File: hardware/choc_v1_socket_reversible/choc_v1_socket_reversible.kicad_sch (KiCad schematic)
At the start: 76 parts, among them J1 Conn_01x12_MountingPin, J2 Conn_01x12_MountingPin, SW00 SW_Push, SW01 SW_Push, SW02 SW_Push, SW03 SW_Push, SW04 SW_Push, SW05 SW_Push, SW10 SW_Push, SW11 SW_Push, SW12 SW_Push, SW13 SW_Push, SW14 SW_Push, SW15 SW_Push, SW20 SW_Push, SW21 SW_Push, SW22 SW_Push, SW23 SW_Push, SW24 SW_Push, SW25 SW_Push, SW30 SW_Push, SW31 SW_Push, SW32 SW_Push, SW33 SW_Push, SW34 SW_Push, SW35 SW_Push, SW36 SW_Push, SW37 SW_Push, U1 CH582, U2 74HC165, U4 74HC165

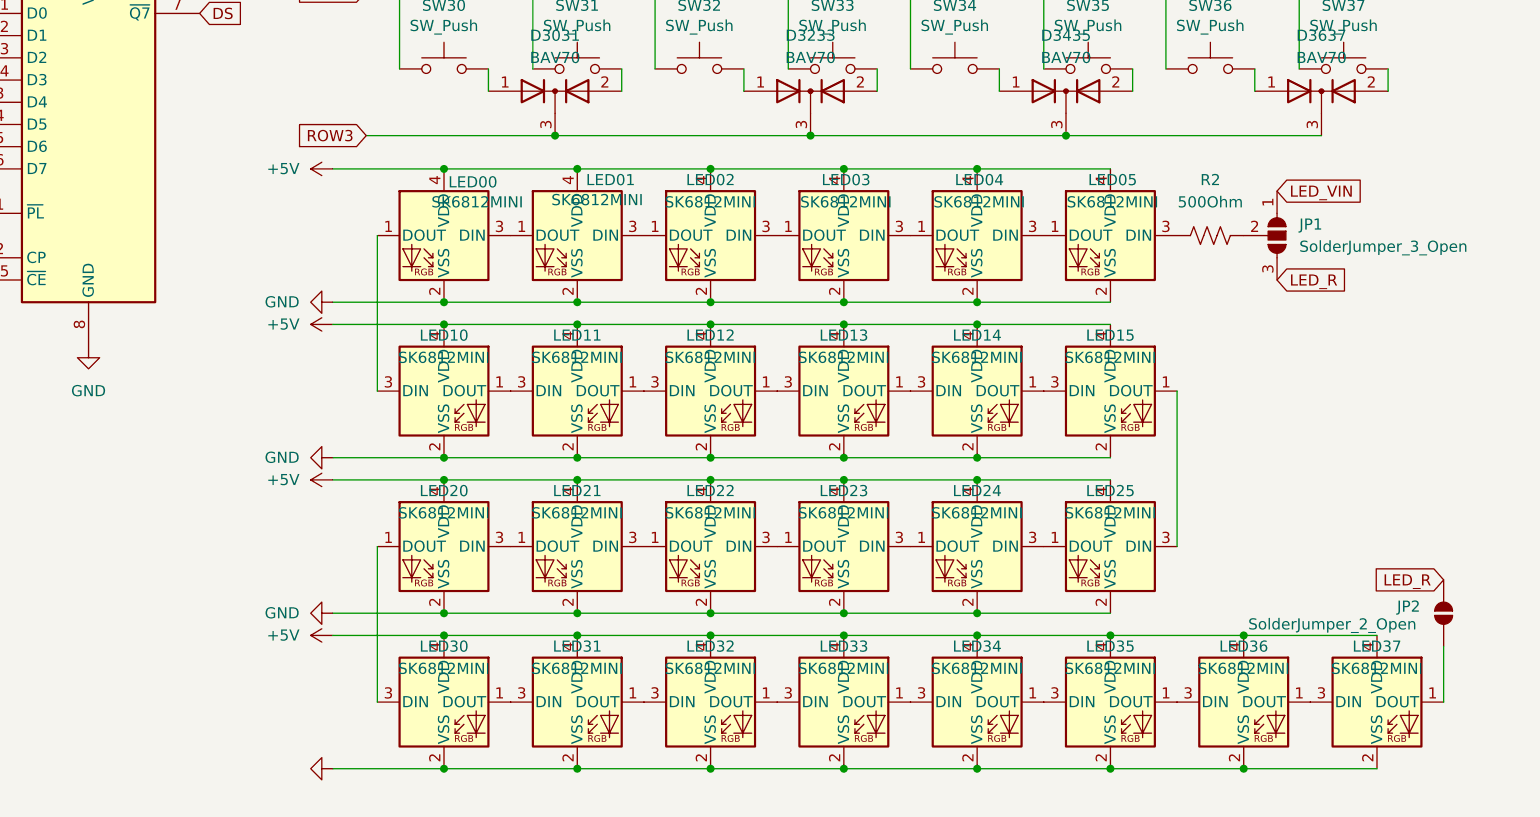
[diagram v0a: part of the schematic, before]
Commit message: Updated schematic and layout, todo: thumb cluster & MCU place and route
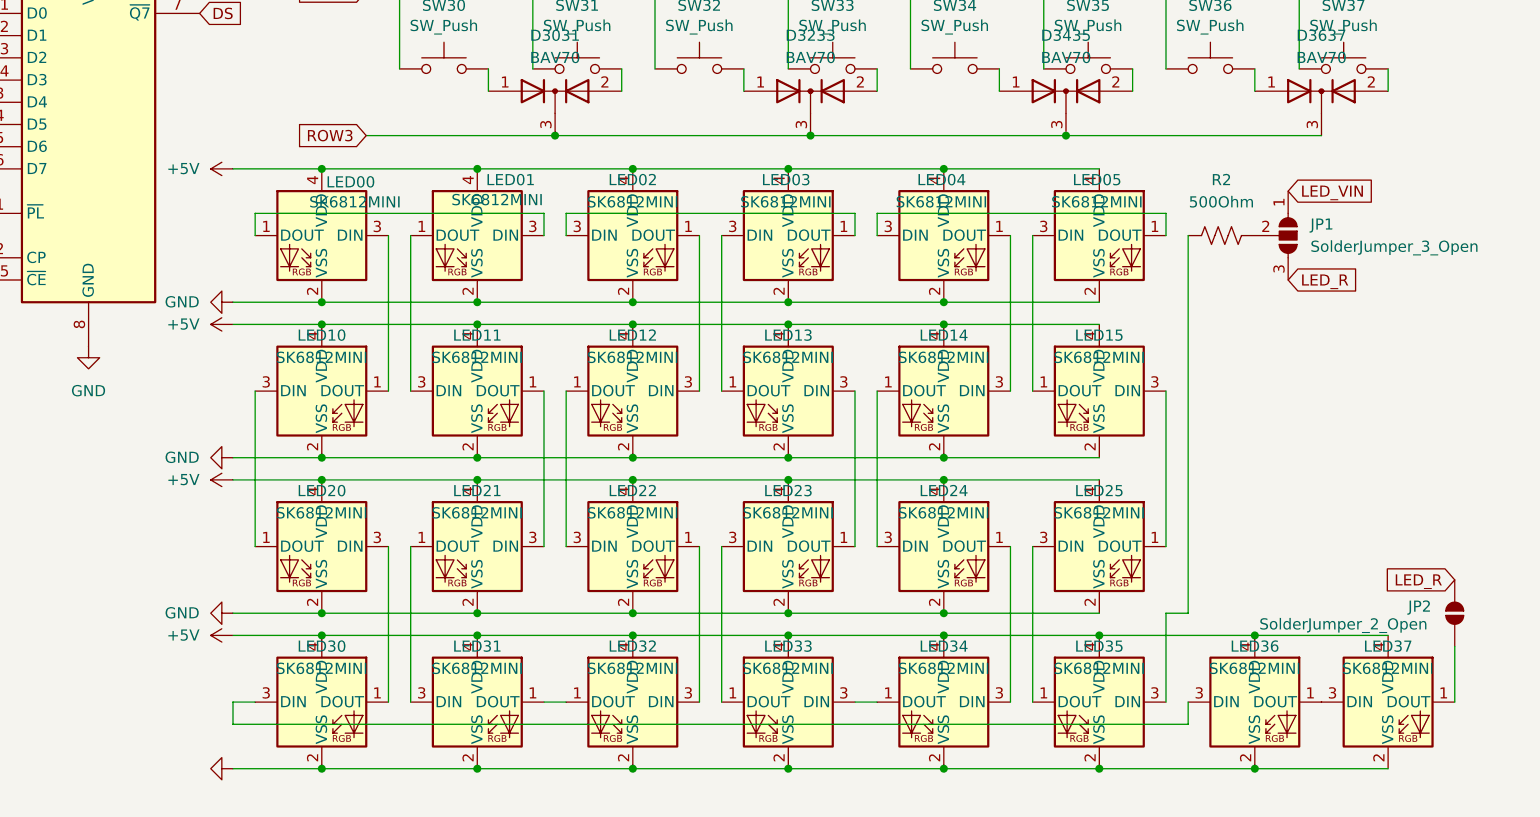
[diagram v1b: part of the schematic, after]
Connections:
- net at LED34.1 (DOUT): now also LED33.3 (DIN); no longer LED35.3 (DIN)
- net at LED34.3 (DIN): now also LED24.1 (DOUT); no longer LED33.1 (DOUT)
- net at LED22.1 (DOUT): now also LED32.3 (DIN); no longer LED21.3 (DIN)
- net at LED22.3 (DIN): now also LED12.1 (DOUT); no longer LED23.1 (DOUT)
- net at LED11.1 (DOUT): now also LED21.3 (DIN); no longer LED12.3 (DIN)
- net at LED11.3 (DIN): now also LED01.1 (DOUT); no longer LED10.1 (DOUT)
- net at LED10.3 (DIN): now also LED20.1 (DOUT); no longer LED00.1 (DOUT)
- net at LED02.1 (DOUT): now also LED12.3 (DIN); no longer LED01.3 (DIN)
- net at LED36.3 (DIN): now also LED30.3 (DIN); no longer LED35.1 (DOUT)
- net at LED13.3 (DIN): now also LED23.1 (DOUT); no longer LED12.1 (DOUT)
- net at LED03.3 (DIN): now also LED13.1 (DOUT); no longer LED04.1 (DOUT)
- net at LED21.1 (DOUT): now also LED31.3 (DIN); no longer LED20.3 (DIN)
- net at LED25.1 (DOUT): now also LED15.3 (DIN); no longer LED24.3 (DIN)
- net at LED25.3 (DIN): now also LED35.1 (DOUT); no longer LED15.1 (DOUT)
- net at LED14.1 (DOUT): now also LED24.3 (DIN); no longer LED15.3 (DIN)
- net at LED14.3 (DIN): now also LED04.1 (DOUT); no longer LED13.1 (DOUT)
- net at LED00.3 (DIN): now also LED10.1 (DOUT); no longer LED01.1 (DOUT)
- net at LED31.1 (DOUT): now also LED32.1 (DOUT); no longer LED32.3 (DIN)
- net at LED30.1 (DOUT): now also LED20.3 (DIN); no longer LED31.3 (DIN)
- net at R2.1: now also LED35.3 (DIN); no longer LED05.3 (DIN)
- net at LED23.3 (DIN): now also LED33.1 (DOUT); no longer LED24.1 (DOUT)
- new net: LED00.1 (DOUT), LED01.3 (DIN)
- new net: LED05.3 (DIN), LED15.1 (DOUT)
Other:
- moved on the sheet: JP1, JP2, LED00, LED01, LED02, LED04, LED05, LED10, LED11, LED12, LED14, LED15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

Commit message: Updated reference
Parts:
- renumbered RN2 to RN_LEFT1, RN1 to RN_RIGHT1, U2 to SR_LEFT1, U4 to SR_RIGHT1
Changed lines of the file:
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@@
 		(dnp no)
 		(fields_autoplaced yes)
-		(property "Reference" "U2"
+		(property "Reference" "SR_LEFT1"
 			(at 63.1541 66.04 0)
 			(effects
@@
 			(project ""
 				(path "/1dbf748e-8163-44a2-a238-31b19fe70046"
-					(reference "U2")
+					(reference "SR_LEFT1")
 					(unit 1)
 				)
@@
 		(dnp no)
 		(fields_autoplaced yes)
-		(property "Reference" "U4"
+		(property "Reference" "SR_RIGHT1"
 			(at 127.9241 66.04 0)
 			(effects
@@
 			(project "new_kbd_right_hand"
 				(path "/1dbf748e-8163-44a2-a238-31b19fe70046"
-					(reference "U4")
+					(reference "SR_RIGHT1")
 					(unit 1)
 				)
@@
 		(dnp no)
 		(fields_autoplaced yes)
-		(property "Reference" "RN1"
+		(property "Reference" "RN_RIGHT1"
 			(at 90.17 62.2299 0)
 			(effects
@@
 			(project "kbd"
 				(path "/1dbf748e-8163-44a2-a238-31b19fe70046"
-					(reference "RN1")
+					(reference "RN_RIGHT1")
 					(unit 1)
 				)
@@
 		(dnp no)
 		(fields_autoplaced yes)
-		(property "Reference" "RN2"
+		(property "Reference" "RN_LEFT1"
 			(at 24.13 62.2299 0)
 			(effects
@@
 			(project ""
 				(path "/1dbf748e-8163-44a2-a238-31b19fe70046"
-					(reference "RN2")
+					(reference "RN_LEFT1")
 					(unit 1)
 				)

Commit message: Generated gerber
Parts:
- renumbered J2 to J_LEFT1, J1 to J_RIGHT1
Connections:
- net +3V3: now also J_LEFT1.8 (Pin_8), J_RIGHT1.5 (Pin_5); no longer J_LEFT1.9 (Pin_9), J_RIGHT1.4 (Pin_4)
- net DS: now also J_LEFT1.5 (Pin_5), J_RIGHT1.8 (Pin_8); no longer J_LEFT1.8 (Pin_8), J_RIGHT1.5 (Pin_5)
- net LED_R: now also J_LEFT1.9 (Pin_9), J_RIGHT1.4 (Pin_4); no longer J_LEFT1.5 (Pin_5), J_RIGHT1.8 (Pin_8)
- net ROW0: now also J_LEFT1.7 (Pin_7), J_RIGHT1.6 (Pin_6); no longer J_LEFT1.4 (Pin_4), J_RIGHT1.9 (Pin_9)
- net ROW1: now also J_LEFT1.6 (Pin_6), J_RIGHT1.7 (Pin_7); no longer J_LEFT1.3 (Pin_3), J_RIGHT1.10 (Pin_10)
- net SCK0: now also J_LEFT1.3 (Pin_3), J_RIGHT1.10 (Pin_10); no longer J_LEFT1.7 (Pin_7), J_RIGHT1.6 (Pin_6)
- net SCS: now also J_LEFT1.4 (Pin_4), J_RIGHT1.9 (Pin_9); no longer J_LEFT1.6 (Pin_6), J_RIGHT1.7 (Pin_7)
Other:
- moved on the sheet: J_LEFT1, J_RIGHT1
